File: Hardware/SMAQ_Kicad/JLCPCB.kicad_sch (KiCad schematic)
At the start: 80 parts, among them J1 USB_B_Micro, J2 Screw_Term, J3 Conn_01x06_Pin, J4 Conn_01x02_Pin, K1 Relay_SPST-NO, Q1 NPN, SW2 SW_DIP_x01, SW3 SW_Push, SW6 Button_PTS645SL43SMTR92LFS, T1 H1102NLT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

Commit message: added footprint for JST and Reset Button
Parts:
- SW6: footprint SMAQ_Footprints:Button_PTS645SL43SMTR92LFS -> SMAQ_FOOTPRINTS:PTS645SL43SMTR92LFS_CNK
- U4: footprint SMAQ_Footprints:CONN_SM05B-GHS-TBLFSN_JST -> SMAQ_FOOTPRINTS:CONN_SM05B-GHS-TBLFSN_JST
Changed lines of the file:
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@@
       (effects (font (size 1.524 1.524)) hide)
     )
-    (property "Footprint" "SMAQ_Footprints:Button_PTS645SL43SMTR92LFS" (at 42.418 54.356 0)
+    (property "Footprint" "SMAQ_FOOTPRINTS:PTS645SL43SMTR92LFS_CNK" (at 42.418 54.356 0)
       (effects (font (size 1.27 1.27) italic) hide)
     )
@@
       (effects (font (size 1.27 1.27)))
     )
-    (property "Footprint" "SMAQ_Footprints:CONN_SM05B-GHS-TBLFSN_JST" (at 280.67 58.42 0)
-      (effects (font (size 1.27 1.27)) hide)
-    )
+    (property "Footprint" "SMAQ_FOOTPRINTS:CONN_SM05B-GHS-TBLFSN_JST" (at 280.67 58.42 0)
+      (effects (font (size 1.27 1.27)) hide)
+    )

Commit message: footprints added
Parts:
- D1: footprint (none) -> SMAQ_FOOTPRINTS:LED_LTST-C194K-0603_1P6X0P8X0P3_LTO
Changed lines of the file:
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@@
       (effects (font (size 1.27 1.27)) (justify left) hide)
     )
-    (property "Footprint" "" (at 227.33 175.26 90)
+    (property "Footprint" "SMAQ_FOOTPRINTS:LED_LTST-C194K-0603_1P6X0P8X0P3_LTO" (at 227.33 175.26 90)
       (effects (font (size 1.27 1.27)) hide)
     )

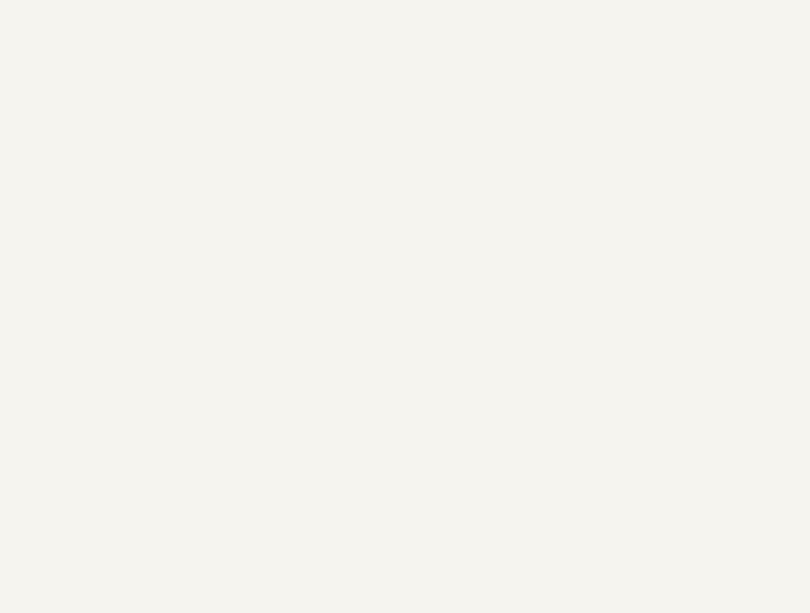
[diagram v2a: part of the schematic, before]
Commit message: Added RJ45 connector
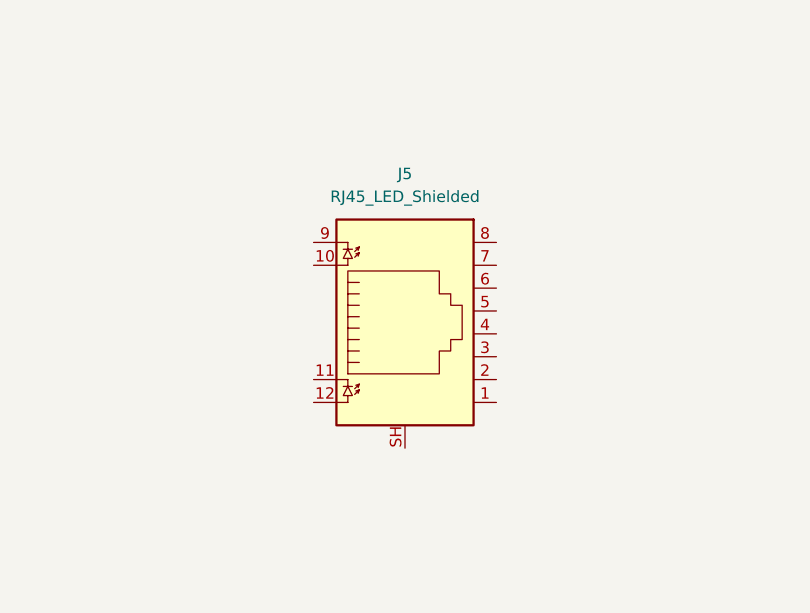
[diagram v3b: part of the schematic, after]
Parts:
- added J5: RJ45_LED_Shielded, symbol Connector:RJ45_LED_Shielded
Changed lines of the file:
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@@
+    )
+  )
+  (symbol (lib_id "Connector:RJ45_LED_Shielded") (at 312.42 492.76 0) (unit 1)
+    (in_bom yes) (on_board yes) (dnp no) (fields_autoplaced)
+    (property "Reference" "J5" (at 312.42 474.98 0)
+      (effects (font (size 1.27 1.27)))
+    )
+    (property "Value" "RJ45_LED_Shielded" (at 312.42 477.52 0)
+      (effects (font (size 1.27 1.27)))
+    )
+    (property "Footprint" "" (at 312.42 492.125 90)
+      (effects (font (size 1.27 1.27)) hide)
+    )
+    (property "Datasheet" "~" (at 312.42 492.125 90)
+      (effects (font (size 1.27 1.27)) hide)
+    )
+    (pin "4")
+    (pin "7")
+    (pin "8")
+    (pin "1")
+    (pin "3")
+    (pin "11")
+    (pin "6")
+    (pin "5")
+    (pin "10")
+    (pin "SH")
+    (pin "2")
+    (pin "12")
+    (pin "9")
+    (instances
+      (project "JLCPCB"
+        (path "/0b3bcc63-e416-4b07-b3bc-df0dd7f6b9c6"
+          (reference "J5") (unit 1)
+        )
+      )
     )
   )
